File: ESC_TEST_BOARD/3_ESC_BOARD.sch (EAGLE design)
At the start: 34 parts

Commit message: Finshing out circuit board
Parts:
- added BOOT: SWITCH, DiscreteComponents:SWITCH
- added C11, C12, C13, C14, C15, C16, C17: (no value), rcl:C-EUC0603
- added C18, C19, C20: (no value), PowerComponents:C-ALUMINUM(330UF)
- added C21, C22, C23: 0.1uF, SparkFun-Capacitors:0.1UF-0603-25V-(+80/-20%)
- added J3: AVR_SPI_PROG_3X2NS, SparkFun-Connectors:AVR_SPI_PROG_3X2NS
- added JP1, JP10, JP11, JP12, JP13, JP14, JP15, JP2, JP3, JP4, JP5, JP6, JP7, JP8, JP9: (no value), pinhead:PINHD-1X1
- added R10, R11, R12: (no value), SparkFun-Resistors:RESISTOR0603
- added U2: ATMEGA328P_TQFP, SparkFun-IC-Microcontroller:ATMEGA328P_TQFP
- added Y2: (no value), SparkFun-Clocks:CRYSTALPTH-HC49US
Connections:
- removed net CLK: U$4.CLK
- removed net CS/SHDN: U$4.CS/SHDN
- removed net DIN: U$4.DIN
- removed net DOUT: U$4.DOUT
- new net CS: TO-MICRO.4, U$4.CS/SHDN, U2.PB2(SS/OC1B)
- new net IN: U2.PD1(TXD)
- new net MISO: J3.1, TO-MICRO.2, U$4.DOUT, U2.PB4(MISO)
- new net MOSI: J3.4, TO-MICRO.3, U$4.DIN, U2.PB3(MOSI/OC2)
- new net N$14: C16.1, U2.PB6(XTAL1/TOSC1), Y2.2
- new net N$15: C17.1, U2.PB7(XTAL2/TOSC2), Y2.1
- new net N$24: JP9.1
- new net N$25: JP10.1
- new net RESET: BOOT.P$2, C11.2, J3.5, R10.1, U2.PC6(/RESET)
- new net SCK: J3.3, TO-MICRO.1, U$4.CLK, U2.PB5(SCK)
- new net SCL: JP8.1, R11.1, U2.PC5(ADC5/SCL)
- new net SDA: JP7.1, R12.1, U2.PC4(ADC4/SDA)
- net +12V: now also JP13.1
- net +5V: now also C12.1, C13.1, C14.1, C15.1, J3.2, JP11.1, JP12.1, R10.2, R11.2, R12.2, U2.AREF, U2.AVCC, U2.VCC@4, U2.VCC@6
- net ANALOG_1: now also JP1.1
- net ANALOG_2: now also JP2.1
- net ANALOG_3: now also JP3.1
- net ANALOG_4: now also JP4.1
- net ANALOG_5: now also JP5.1
- net ANALOG_6: now also JP6.1
- net ESC1: now also C18.+, C21.1
- net ESC2: now also C19.+, C22.1
- net ESC3: now also C20.+, C23.1
- net GND: now also BOOT.P$1, C11.1, C12.2, C13.2, C14.2, C15.2, C16.2, C17.2, C18.-, C19.-, C20.-, C21.2, C22.2, C23.2, J3.6, JP14.1, JP15.1, U2.AGND, U2.GND@3, U2.GND@5
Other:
- moved on the sheet: J1, J2, PWM_HEADER, TO-MICRO

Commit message: Updating ESC Test Board
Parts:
- removed JP10, JP11, JP15, JP9: (no value), pinhead:PINHD-1X1
- removed TO-MICRO: (no value), con-lstb:MA04-1
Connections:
- removed net IN: U2.PD1(TXD)
- removed net N$24: JP9.1
- removed net N$25: JP10.1
- net +5V: no longer JP11.1
- net CS: no longer TO-MICRO.4
- net GND: no longer JP15.1
- net MISO: no longer TO-MICRO.2
- net MOSI: no longer TO-MICRO.3
- net SCK: no longer TO-MICRO.1
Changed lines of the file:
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@@
 <part name="P+9" library="supply1" library_urn="urn:adsk.eagle:library:371" deviceset="+5V" device=""/>
 <part name="GND20" library="SparkFun-PowerSymbols" deviceset="GND" device=""/>
-<part name="TO-MICRO" library="con-lstb" library_urn="urn:adsk.eagle:library:162" deviceset="MA04-1" device="" package3d_urn="urn:adsk.eagle:package:8337/1"/>
 <part name="C7" library="SparkFun-Capacitors" deviceset="0.1UF" device="-0603-25V-(+80/-20%)" value="0.1uF"/>
 <part name="GND21" library="SparkFun-PowerSymbols" deviceset="GND" device=""/>
@@
 <part name="JP7" library="pinhead" library_urn="urn:adsk.eagle:library:325" deviceset="PINHD-1X1" device="" package3d_urn="urn:adsk.eagle:package:22485/1"/>
 <part name="JP8" library="pinhead" library_urn="urn:adsk.eagle:library:325" deviceset="PINHD-1X1" device="" package3d_urn="urn:adsk.eagle:package:22485/1"/>
-<part name="JP9" library="pinhead" library_urn="urn:adsk.eagle:library:325" deviceset="PINHD-1X1" device="" package3d_urn="urn:adsk.eagle:package:22485/1"/>
-<part name="JP10" library="pinhead" library_urn="urn:adsk.eagle:library:325" deviceset="PINHD-1X1" device="" package3d_urn="urn:adsk.eagle:package:22485/1"/>
-<part name="JP11" library="pinhead" library_urn="urn:adsk.eagle:library:325" deviceset="PINHD-1X1" device="" package3d_urn="urn:adsk.eagle:package:22485/1"/>
 <part name="JP12" library="pinhead" library_urn="urn:adsk.eagle:library:325" deviceset="PINHD-1X1" device="" package3d_urn="urn:adsk.eagle:package:22485/1"/>
 <part name="JP13" library="pinhead" library_urn="urn:adsk.eagle:library:325" deviceset="PINHD-1X1" device="" package3d_urn="urn:adsk.eagle:package:22485/1"/>
 <part name="JP14" library="pinhead" library_urn="urn:adsk.eagle:library:325" deviceset="PINHD-1X1" device="" package3d_urn="urn:adsk.eagle:package:22485/1"/>
-<part name="JP15" library="pinhead" library_urn="urn:adsk.eagle:library:325" deviceset="PINHD-1X1" device="" package3d_urn="urn:adsk.eagle:package:22485/1"/>
 <part name="P+10" library="supply1" library_urn="urn:adsk.eagle:library:371" deviceset="+5V" device=""/>
 <part name="GND34" library="SparkFun-PowerSymbols" deviceset="GND" device=""/>
@@
 <instance part="P+9" gate="1" x="358.14" y="116.84"/>
 <instance part="GND20" gate="1" x="373.38" y="76.2"/>
-<instance part="TO-MICRO" gate="1" x="370.84" y="93.98" rot="R180"/>
 <instance part="C7" gate="G$1" x="317.5" y="175.26"/>
 <instance part="GND21" gate="1" x="317.5" y="167.64"/>
@@
 <instance part="JP7" gate="G$1" x="40.64" y="190.5" rot="R180"/>
 <instance part="JP8" gate="G$1" x="40.64" y="180.34" rot="R180"/>
-<instance part="JP9" gate="G$1" x="40.64" y="170.18" rot="R180"/>
-<instance part="JP10" gate="G$1" x="40.64" y="160.02" rot="R180"/>
-<instance part="JP11" gate="G$1" x="66.04" y="200.66" rot="R180"/>
 <instance part="JP12" gate="G$1" x="66.04" y="190.5" rot="R180"/>
 <instance part="JP13" gate="G$1" x="66.04" y="180.34" rot="R180"/>
 <instance part="JP14" gate="G$1" x="66.04" y="170.18" rot="R180"/>
-<instance part="JP15" gate="G$1" x="66.04" y="160.02" rot="R180"/>
 <instance part="P+10" gate="1" x="88.9" y="208.28"/>
 <instance part="GND34" gate="1" x="86.36" y="152.4"/>
@@
 <label x="73.66" y="170.18" size="1.778" layer="95"/>
 <pinref part="GND34" gate="1" pin="GND"/>
-<wire x1="86.36" y1="170.18" x2="86.36" y2="160.02" width="0.1524" layer="91"/>
-<pinref part="JP15" gate="G$1" pin="1"/>
-<wire x1="86.36" y1="160.02" x2="86.36" y2="154.94" width="0.1524" layer="91"/>
-<wire x1="68.58" y1="160.02" x2="86.36" y2="160.02" width="0.1524" layer="91"/>
-<label x="73.66" y="160.02" size="1.778" layer="95"/>
-<junction x="86.36" y="160.02"/>
+<wire x1="86.36" y1="170.18" x2="86.36" y2="154.94" width="0.1524" layer="91"/>
 </segment>
 </net>
@@
 </segment>
 <segment>
-<pinref part="JP11" gate="G$1" pin="1"/>
-<wire x1="68.58" y1="200.66" x2="88.9" y2="200.66" width="0.1524" layer="91"/>
-<label x="73.66" y="200.66" size="1.778" layer="95"/>
 <pinref part="P+10" gate="1" pin="+5V"/>
-<wire x1="88.9" y1="200.66" x2="88.9" y2="205.74" width="0.1524" layer="91"/>
 <pinref part="JP12" gate="G$1" pin="1"/>
 <wire x1="68.58" y1="190.5" x2="88.9" y2="190.5" width="0.1524" layer="91"/>
 <label x="73.66" y="190.5" size="1.778" layer="95"/>
-<wire x1="88.9" y1="190.5" x2="88.9" y2="200.66" width="0.1524" layer="91"/>
-<junction x="88.9" y="200.66"/>
+<wire x1="88.9" y1="190.5" x2="88.9" y2="205.74" width="0.1524" layer="91"/>
 </segment>
 <segment>
@@
 <pinref part="U$4" gate="G$1" pin="CS/SHDN"/>
 <wire x1="350.52" y1="91.44" x2="363.22" y2="91.44" width="0.1524" layer="91"/>
-<pinref part="TO-MICRO" gate="1" pin="4"/>
 <label x="360.68" y="91.44" size="1.778" layer="95"/>
 </segment>
@@
 <wire x1="523.24" y1="106.68" x2="535.94" y2="106.68" width="0.1524" layer="91"/>
 <label x="528.32" y="106.68" size="1.778" layer="95"/>
-</segment>
-</net>
-<net name="IN" class="0">
-<segment>
-<pinref part="U2" gate="U$1" pin="PD1(TXD)"/>
-<wire x1="523.24" y1="132.08" x2="543.56" y2="132.08" width="0.1524" layer="91"/>
-<label x="538.48" y="132.08" size="1.778" layer="95"/>
 </segment>
 </net>
@@
 <pinref part="U$4" gate="G$1" pin="DIN"/>
 <wire x1="350.52" y1="93.98" x2="363.22" y2="93.98" width="0.1524" layer="91"/>
-<pinref part="TO-MICRO" gate="1" pin="3"/>
 <label x="355.6" y="93.98" size="1.778" layer="95"/>
 </segment>
@@
 <pinref part="U$4" gate="G$1" pin="DOUT"/>
 <wire x1="350.52" y1="96.52" x2="363.22" y2="96.52" width="0.1524" layer="91"/>
-<pinref part="TO-MICRO" gate="1" pin="2"/>
 <label x="355.6" y="96.52" size="1.778" layer="95"/>
 </segment>
@@
 <pinref part="U$4" gate="G$1" pin="CLK"/>
 <wire x1="350.52" y1="99.06" x2="363.22" y2="99.06" width="0.1524" layer="91"/>
-<pinref part="TO-MICRO" gate="1" pin="1"/>
 <label x="355.6" y="99.06" size="1.778" layer="95"/>
 </segment>
@@
 </segment>
 </net>
-<net name="N$24" class="0">
-<segment>
-<pinref part="JP9" gate="G$1" pin="1"/>
-<wire x1="43.18" y1="170.18" x2="53.34" y2="170.18" width="0.1524" layer="91"/>
-<label x="48.26" y="170.18" size="1.778" layer="95"/>
-</segment>
-</net>
-<net name="N$25" class="0">
-<segment>
-<pinref part="JP10" gate="G$1" pin="1"/>
-<wire x1="43.18" y1="160.02" x2="53.34" y2="160.02" width="0.1524" layer="91"/>
-<label x="48.26" y="160.02" size="1.778" layer="95"/>
-</segment>
-</net>

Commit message: Updating ESC Test Board
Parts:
- removed JP7, JP8: (no value), pinhead:PINHD-1X1
- added SV2: (no value), con-lsta:FE06-2
- renumbered BOOT to RESET
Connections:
- new net +3V3: R11.2, R12.2
- new net PB0: SV2.6, U2.PB0(ICP)
- new net PD3: SV2.1, U2.PD3(INT1)
- new net PD4: SV2.2, U2.PD4(XCK/T0)
- new net PD5: SV2.3, U2.PD5(T1)
- new net PD6: SV2.4, U2.PD6(AIN0)
- new net PD7: SV2.5, U2.PD7(AIN1)
- net +5V: no longer R11.2, R12.2
- net CS: now also SV2.7
- net MISO: now also SV2.9
- net MOSI: now also SV2.8
- net SCK: now also SV2.10
- net SCL: now also SV2.12; no longer JP8.1
- net SDA: now also SV2.11; no longer JP7.1

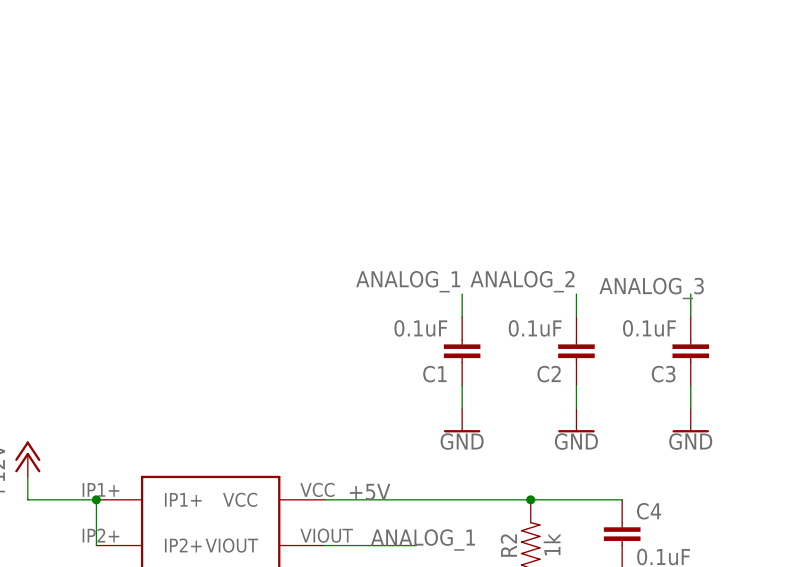
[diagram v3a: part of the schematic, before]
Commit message: Almost done with initial routing
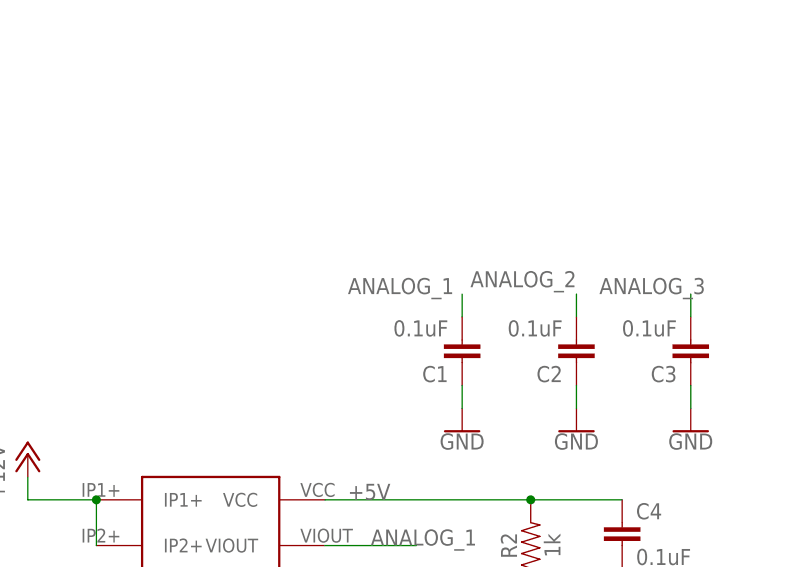
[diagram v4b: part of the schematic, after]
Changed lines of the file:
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@@
-</segment>
-<segment>
-<pinref part="C1" gate="G$1" pin="2"/>
-<wire x1="76.2" y1="111.76" x2="76.2" y2="114.3" width="0.1524" layer="91"/>
-<label x="76.2" y="116.84" size="1.778" layer="95" rot="R180"/>
 </segment>
 <segment>
@@
 <label x="22.86" y="200.66" size="1.778" layer="95"/>
 </segment>
+<segment>
+<pinref part="C1" gate="G$1" pin="2"/>
+<wire x1="76.2" y1="111.76" x2="76.2" y2="114.3" width="0.1524" layer="91"/>
+<label x="63.5" y="114.3" size="1.778" layer="95"/>
+</segment>
 </net>
